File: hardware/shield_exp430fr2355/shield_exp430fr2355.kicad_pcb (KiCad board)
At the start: 2 copper layers, 78.4 x 50 mm, 54 parts, among them J1 TI_BOOSTER_40_J1, J10 Conn_01x02_Male, J12 Conn_01x02_Male, J13 Conn_01x02_Male, J14 Conn_01x02_Male, J15 Conn_01x02_Male, J16 Conn_01x02_Male, J17 Conn_01x02_Male, J18 Conn_01x02_Male, J19 Conn_01x02_Male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

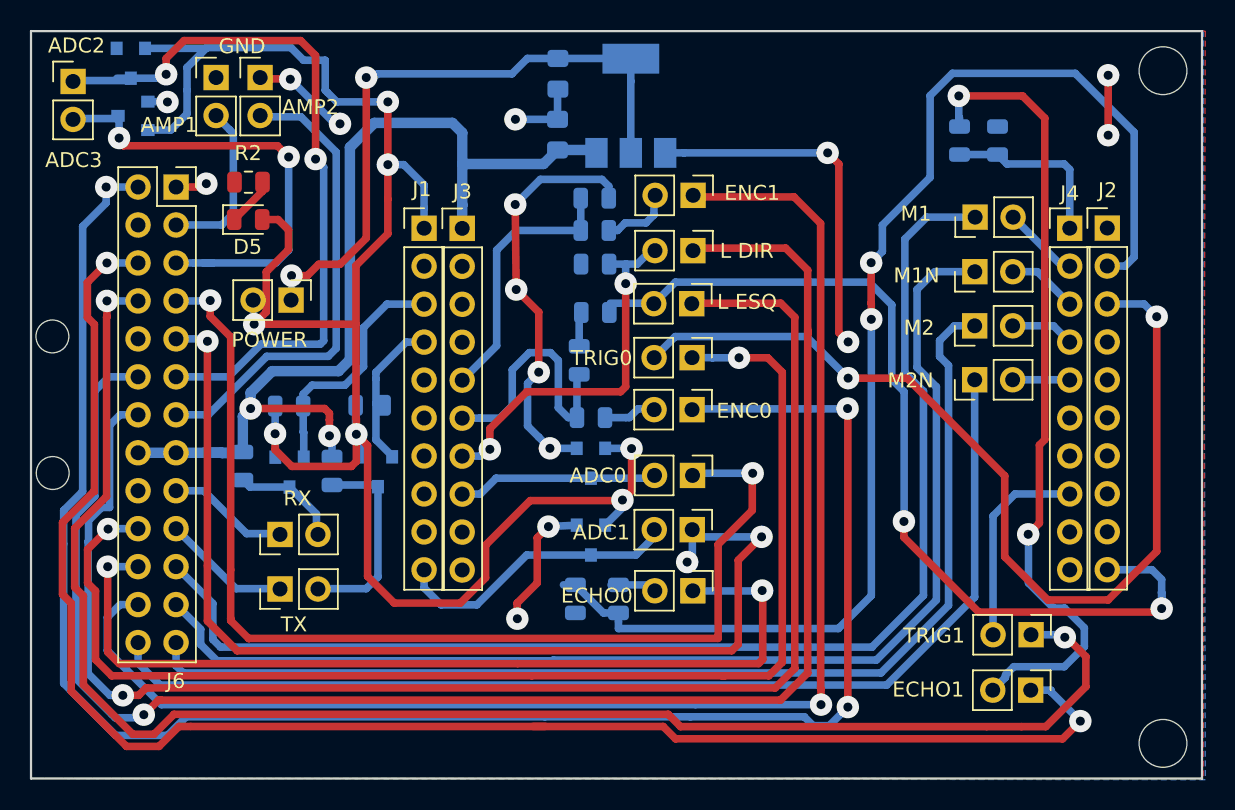
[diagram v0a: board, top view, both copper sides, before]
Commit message: Updated shield hardware, added uart protection!
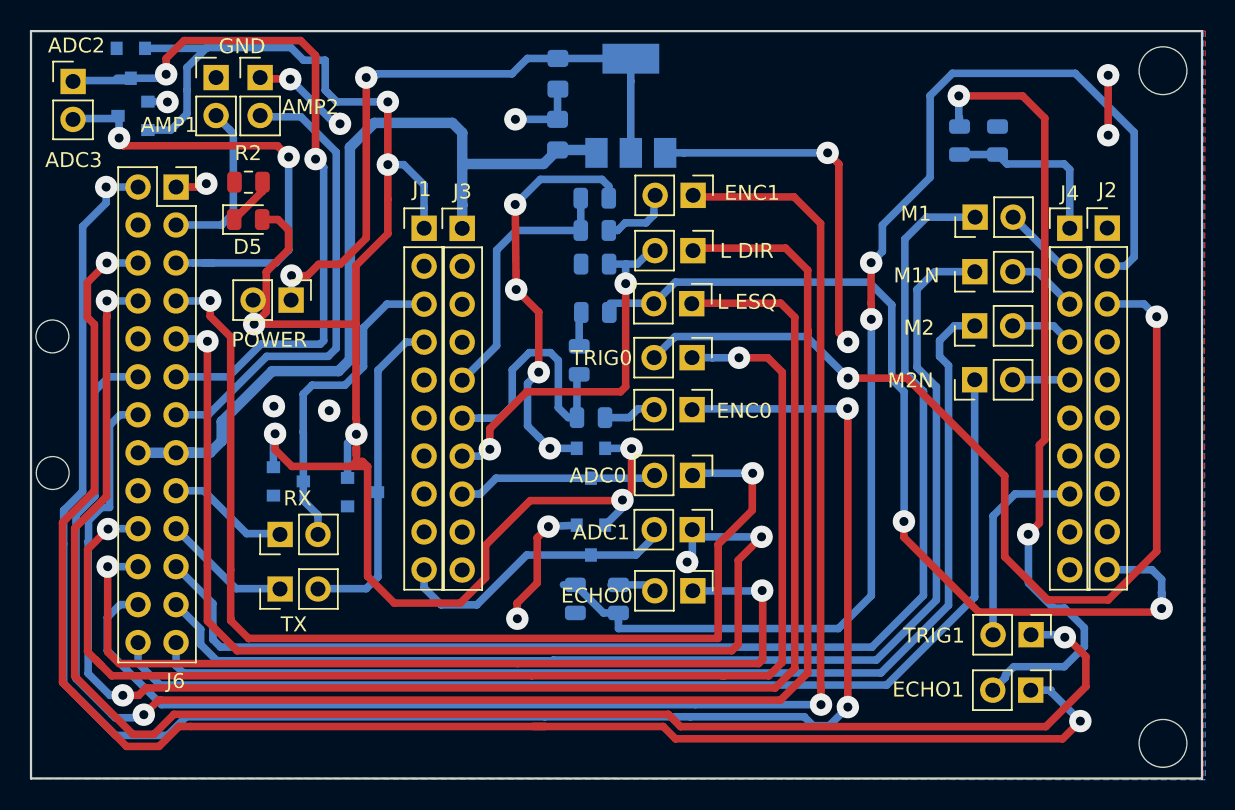
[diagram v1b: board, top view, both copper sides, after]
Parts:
- removed Q1, Q2: 2N7002, Package_TO_SOT_SMD:SOT-23
- removed R12, R13, R14, R15: 2k2, Resistor_SMD:R_0805_2012Metric
- added D6: BAT54S, Package_TO_SOT_SMD:SOT-23, B.Cu at (193.2, 153.7)
- added D7: BAT54S, Package_TO_SOT_SMD:SOT-23, B.Cu at (188.3, 153.0)
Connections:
- J27 pad 2: Tx -> P1.7
- J28 pad 2: Rx -> P1.6
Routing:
- net Tx: track 13.6 -> 0.00 mm
- net P1.7: track 10.7 -> 22.2 mm
- net +5V: track 68.6 -> 57.2 mm, vias 2 -> 0
- net Rx: track 7.25 -> 0.00 mm
- net P1.6: track 16.3 -> 22.0 mm
- net +3V3: track 129.4 -> 127.8 mm
- net GND: vias 15 -> 17
